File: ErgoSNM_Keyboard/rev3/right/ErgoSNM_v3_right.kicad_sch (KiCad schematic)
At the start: 20 parts, among them J1 USB_C_Receptacle_USB2.0, J2 Conn_01x02, J3 Conn_01x08, J4 Conn_01x04, SW1 SW_DPDT_x2, U1 TPS61220DCK

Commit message: Add LDO for USB
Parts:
- added C7, C8: 1uF, Capacitor_SMD:C_0402_1005Metric, symbol Device:C
- added unit 2 of SW1
- added U3: RT9013-33GB, Package_TO_SOT_SMD:SOT-23-5, symbol rp-micro:RT9013-33GB
- R1: value 560k -> 1.2M
- R4: value 200k -> 220k
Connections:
- net +5V: now also C7.1, SW1.4 (A), U3.1 (VIN)
- net GND: now also C7.2, C8.2, SW1.6 (C), U3.2 (GND)
- net VDD: now also C8.1, U3.5 (VOUT)
- new net: SW1.5 (B), U3.3 (EN)
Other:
- note added: "R_{1}=R_{2}*((V_{out}/V_{FB})-1), V_{FB}=0.5V R_{1} 560k, R_{2} 200k: V_{out}=1.9V R_{1} 1.2M, R_{2} 220k: V_{out}=3.2V"
- note removed: "R_{1}=R_{2}*((V_{out}/V_{FB})-1), V_{FB}=0.5V R_{1} 560k, R_{2} 200k: V_{out}=1.9V"
- moved on the sheet: SW1A

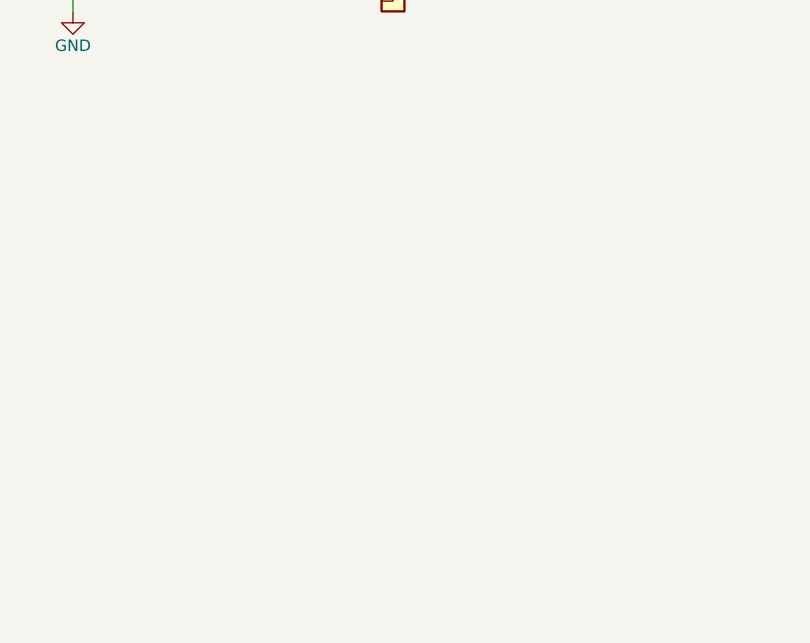
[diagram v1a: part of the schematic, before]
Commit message: Add key-matrix test pointes (2.54mm pin header)
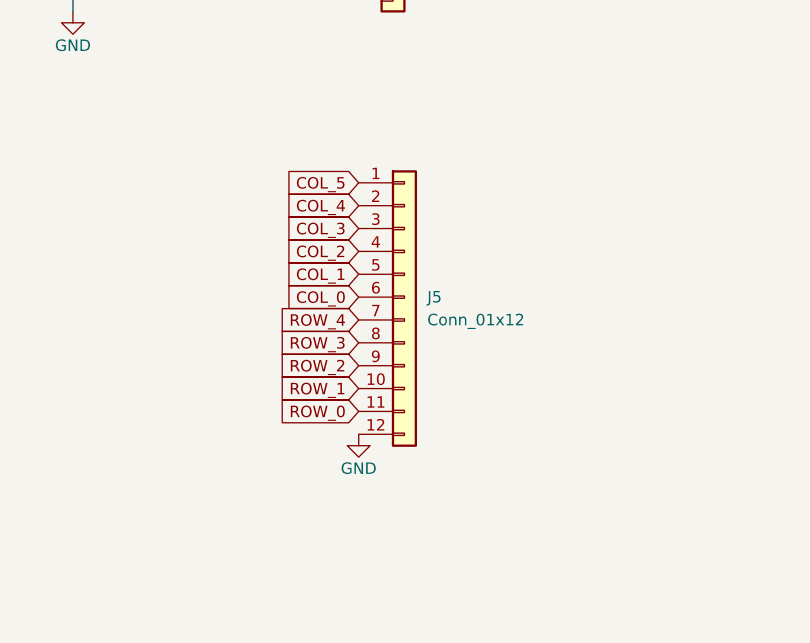
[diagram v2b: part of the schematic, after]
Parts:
- added J5: Conn_01x12, Connector_PinHeader_2.54mm:PinHeader_1x12_P2.54mm_Vertical, symbol Connector_Generic:Conn_01x12
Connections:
- net GND: now also J5.12 (Pin_12)
- new net COL_0: J5.6 (Pin_6)
- new net COL_1: J5.5 (Pin_5)
- new net COL_2: J5.4 (Pin_4)
- new net COL_3: J5.3 (Pin_3)
- new net COL_4: J5.2 (Pin_2)
- new net COL_5: J5.1 (Pin_1)
- new net ROW_0: J5.11 (Pin_11)
- new net ROW_1: J5.10 (Pin_10)
- new net ROW_2: J5.9 (Pin_9)
- new net ROW_3: J5.8 (Pin_8)
- new net ROW_4: J5.7 (Pin_7)
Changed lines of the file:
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@@
     (effects (font (size 1.27 1.27)) (justify left bottom))
   )
+  (global_label "ROW_3" (shape input) (at 72.39 163.83 180) (fields_autoplaced)
+    (effects (font (size 1.27 1.27)) (justify right))
+    (property "Intersheetrefs" "${INTERSHEET_REFS}" (at 63.7479 163.7506 0)
+      (effects (font (size 1.27 1.27)) (justify right) hide)
+    )
+  )
   (global_label "PMW3360_SPI_SCLK" (shape input) (at 69.85 113.03 180) (fields_autoplaced)
     (effects (font (size 1.27 1.27)) (justify right))
@@
     )
   )
+  (global_label "COL_4" (shape input) (at 72.39 148.59 180) (fields_autoplaced)
+    (effects (font (size 1.27 1.27)) (justify right))
+    (property "Intersheetrefs" "${INTERSHEET_REFS}" (at 63.5991 148.59 0)
+      (effects (font (size 1.27 1.27)) (justify right) hide)
+    )
+  )
   (global_label "PMW3360_SPI_MOSI" (shape input) (at 69.85 115.57 180) (fields_autoplaced)
     (effects (font (size 1.27 1.27)) (justify right))
     (property "Intersheetrefs" "${INTERSHEET_REFS}" (at 48.2383 115.57 0)
+      (effects (font (size 1.27 1.27)) (justify right) hide)
+    )
+  )
+  (global_label "COL_2" (shape input) (at 72.39 153.67 180) (fields_autoplaced)
+    (effects (font (size 1.27 1.27)) (justify right))
+    (property "Intersheetrefs" "${INTERSHEET_REFS}" (at 63.5991 153.67 0)
       (effects (font (size 1.27 1.27)) (justify right) hide)
     )
@@
     )
   )
+  (global_label "COL_3" (shape input) (at 72.39 151.13 180) (fields_autoplaced)
+    (effects (font (size 1.27 1.27)) (justify right))
+    (property "Intersheetrefs" "${INTERSHEET_REFS}" (at 63.5991 151.13 0)
+      (effects (font (size 1.27 1.27)) (justify right) hide)
+    )
+  )
   (global_label "PMW3360_SPI_MISO" (shape input) (at 69.85 118.11 180) (fields_autoplaced)
     (effects (font (size 1.27 1.27)) (justify right))
@@
     )
   )
+  (global_label "COL_1" (shape input) (at 72.39 156.21 180) (fields_autoplaced)
+    (effects (font (size 1.27 1.27)) (justify right))
+    (property "Intersheetrefs" "${INTERSHEET_REFS}" (at 63.5991 156.21 0)
+      (effects (font (size 1.27 1.27)) (justify right) hide)
+    )
+  )
+  (global_label "ROW_1" (shape input) (at 72.39 168.91 180) (fields_autoplaced)
+    (effects (font (size 1.27 1.27)) (justify right))
+    (property "Intersheetrefs" "${INTERSHEET_REFS}" (at 63.7479 168.8306 0)
+      (effects (font (size 1.27 1.27)) (justify right) hide)
+    )
+  )
   (global_label "PMW3360_SPI_CS" (shape input) (at 69.85 120.65 180) (fields_autoplaced)
     (effects (font (size 1.27 1.27)) (justify right))
@@
     (effects (font (size 1.27 1.27)) (justify right))
     (property "Intersheetrefs" "${INTERSHEET_REFS}" (at 141.6739 125.73 0)
+      (effects (font (size 1.27 1.27)) (justify right) hide)
+    )
+  )
+  (global_label "ROW_0" (shape input) (at 72.39 171.45 180) (fields_autoplaced)
+    (effects (font (size 1.27 1.27)) (justify right))
+    (property "Intersheetrefs" "${INTERSHEET_REFS}" (at 63.7479 171.3706 0)
+      (effects (font (size 1.27 1.27)) (justify right) hide)
+    )
+  )
+  (global_label "COL_5" (shape input) (at 72.39 146.05 180) (fields_autoplaced)
+    (effects (font (size 1.27 1.27)) (justify right))
+    (property "Intersheetrefs" "${INTERSHEET_REFS}" (at 63.5991 146.05 0)
+      (effects (font (size 1.27 1.27)) (justify right) hide)
+    )
+  )
+  (global_label "ROW_4" (shape input) (at 72.39 161.29 180) (fields_autoplaced)
+    (effects (font (size 1.27 1.27)) (justify right))
+    (property "Intersheetrefs" "${INTERSHEET_REFS}" (at 63.7479 161.2106 0)
       (effects (font (size 1.27 1.27)) (justify right) hide)
     )
@@
     (property "Intersheetrefs" "${INTERSHEET_REFS}" (at 77.9152 46.99 0)
       (effects (font (size 1.27 1.27)) (justify left) hide)
+    )
+  )
+  (global_label "COL_0" (shape input) (at 72.39 158.75 180) (fields_autoplaced)
+    (effects (font (size 1.27 1.27)) (justify right))
+    (property "Intersheetrefs" "${INTERSHEET_REFS}" (at 63.5991 158.75 0)
+      (effects (font (size 1.27 1.27)) (justify right) hide)
+    )
+  )
+  (global_label "ROW_2" (shape input) (at 72.39 166.37 180) (fields_autoplaced)
+    (effects (font (size 1.27 1.27)) (justify right))
+    (property "Intersheetrefs" "${INTERSHEET_REFS}" (at 63.7479 166.2906 0)
+      (effects (font (size 1.27 1.27)) (justify right) hide)
     )
   )
@@
     )
   )
+  (symbol (lib_id "power:GND") (at 72.39 173.99 0) (unit 1)
+    (in_bom yes) (on_board yes) (dnp no)
+    (property "Reference" "#PWR032" (at 72.39 180.34 0)
+      (effects (font (size 1.27 1.27)) hide)
+    )
+    (property "Value" "GND" (at 72.39 177.8 0)
+      (effects (font (size 1.27 1.27)))
+    )
+    (property "Footprint" "" (at 72.39 173.99 0)
+      (effects (font (size 1.27 1.27)) hide)
+    )
+    (property "Datasheet" "" (at 72.39 173.99 0)
+      (effects (font (size 1.27 1.27)) hide)
+    )
+    (pin "1")
+    (instances
+      (project "ErgoSNM_v3_right"
+        (path "/94fd6fa5-abea-4c62-b80d-3b080722228a"
+          (reference "#PWR032") (unit 1)
+        )
+      )
+    )
+  )
   (symbol (lib_id "Device:Polyfuse") (at 69.85 33.02 90) (unit 1)
     (in_bom yes) (on_board yes) (dnp no)
@@
         )
       )
+    )
+  )
+  (symbol (lib_id "Connector_Generic:Conn_01x12") (at 77.47 158.75 0) (unit 1)
+    (in_bom yes) (on_board yes) (dnp no) (fields_autoplaced)
+    (property "Reference" "J5" (at 80.01 158.75 0)
+      (effects (font (size 1.27 1.27)) (justify left))
+    )
+    (property "Value" "Conn_01x12" (at 80.01 161.29 0)
+      (effects (font (size 1.27 1.27)) (justify left))
+    )
+    (property "Footprint" "Connector_PinHeader_2.54mm:PinHeader_1x12_P2.54mm_Vertical" (at 77.47 158.75 0)
+      (effects (font (size 1.27 1.27)) hide)
+    )
+    (property "Datasheet" "~" (at 77.47 158.75 0)
+      (effects (font (size 1.27 1.27)) hide)
+    )
+    (pin "1")
+    (pin "10")
+    (pin "11")
+    (pin "12")
+    (pin "2")
+    (pin "3")
+    (pin "4")
+    (pin "5")
+    (pin "6")
+    (pin "7")
+    (pin "8")
+    (pin "9")
+    (instances
+      (project "ErgoSNM_v3_right"
+        (path "/94fd6fa5-abea-4c62-b80d-3b080722228a"
+          (reference "J5") (unit 1)
+        )
+      )

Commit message: Update submodule
Update submodule

Update switch footprint
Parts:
- renumbered C7 to C1, C8 to C2, C2 to C3, C1 to C4, J4 to J3, J3 to J4, R2 to R1, R3 to R2, R1 to R3, U3 to U1, U1 to U2
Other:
- moved on the sheet: J2, J4, J5, SW1A
